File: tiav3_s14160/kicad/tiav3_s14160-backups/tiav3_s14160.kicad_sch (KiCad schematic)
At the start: 24 parts, among them J1 SSQ-103-01-G-D, J2 Conn_Coaxial, J3 Snibbor Inc LOGO, J4 Bennett close LOGO, U1 OPA847IDBVT

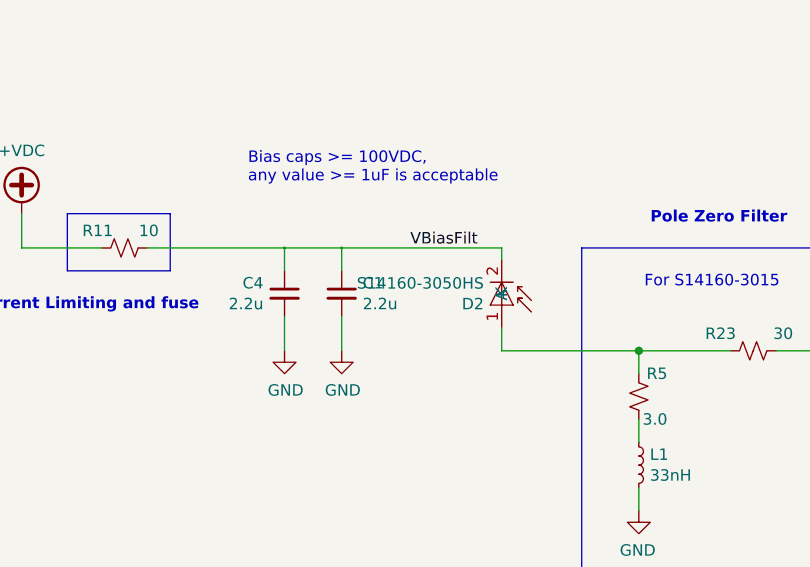
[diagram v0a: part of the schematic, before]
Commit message: updating s14160-3050HS footprint
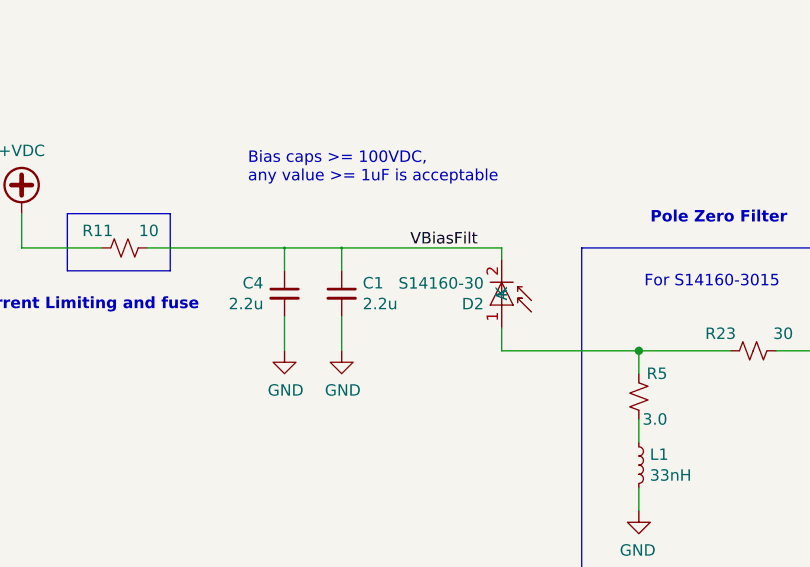
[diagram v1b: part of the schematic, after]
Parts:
- D2: value S14160-3050HS -> S14160-30; footprint footprints:S14160-3050HS -> footprints:S14160-30
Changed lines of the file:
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@@
 			)
 		)
-		(property "Value" "S14160-3050HS"
+		(property "Value" "S14160-30"
 			(at 86.9187 100.4507 90)
 			(effects
@@
 			)
 		)
-		(property "Footprint" "footprints:S14160-3050HS"
+		(property "Footprint" "footprints:S14160-30"
 			(at 93.345 102.87 0)
 			(effects
